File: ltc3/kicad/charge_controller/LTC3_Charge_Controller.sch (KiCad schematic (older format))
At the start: 120 parts, among them P1 MicroFit header, P3 XH header, P4 MicroFit header, P5 XH header, P6 XH header, Q1 ZVN4525E6, Q2 BSC028N06NS, Q3 BSC028N06NS, Q4 BSC028N06NS, Q5 BSC028N06NS, Q6 ZVP3310F, Q7 MMBT5550L, U1 PI2127, U2 PI2127, U3 LT8490, U4 LTC2990

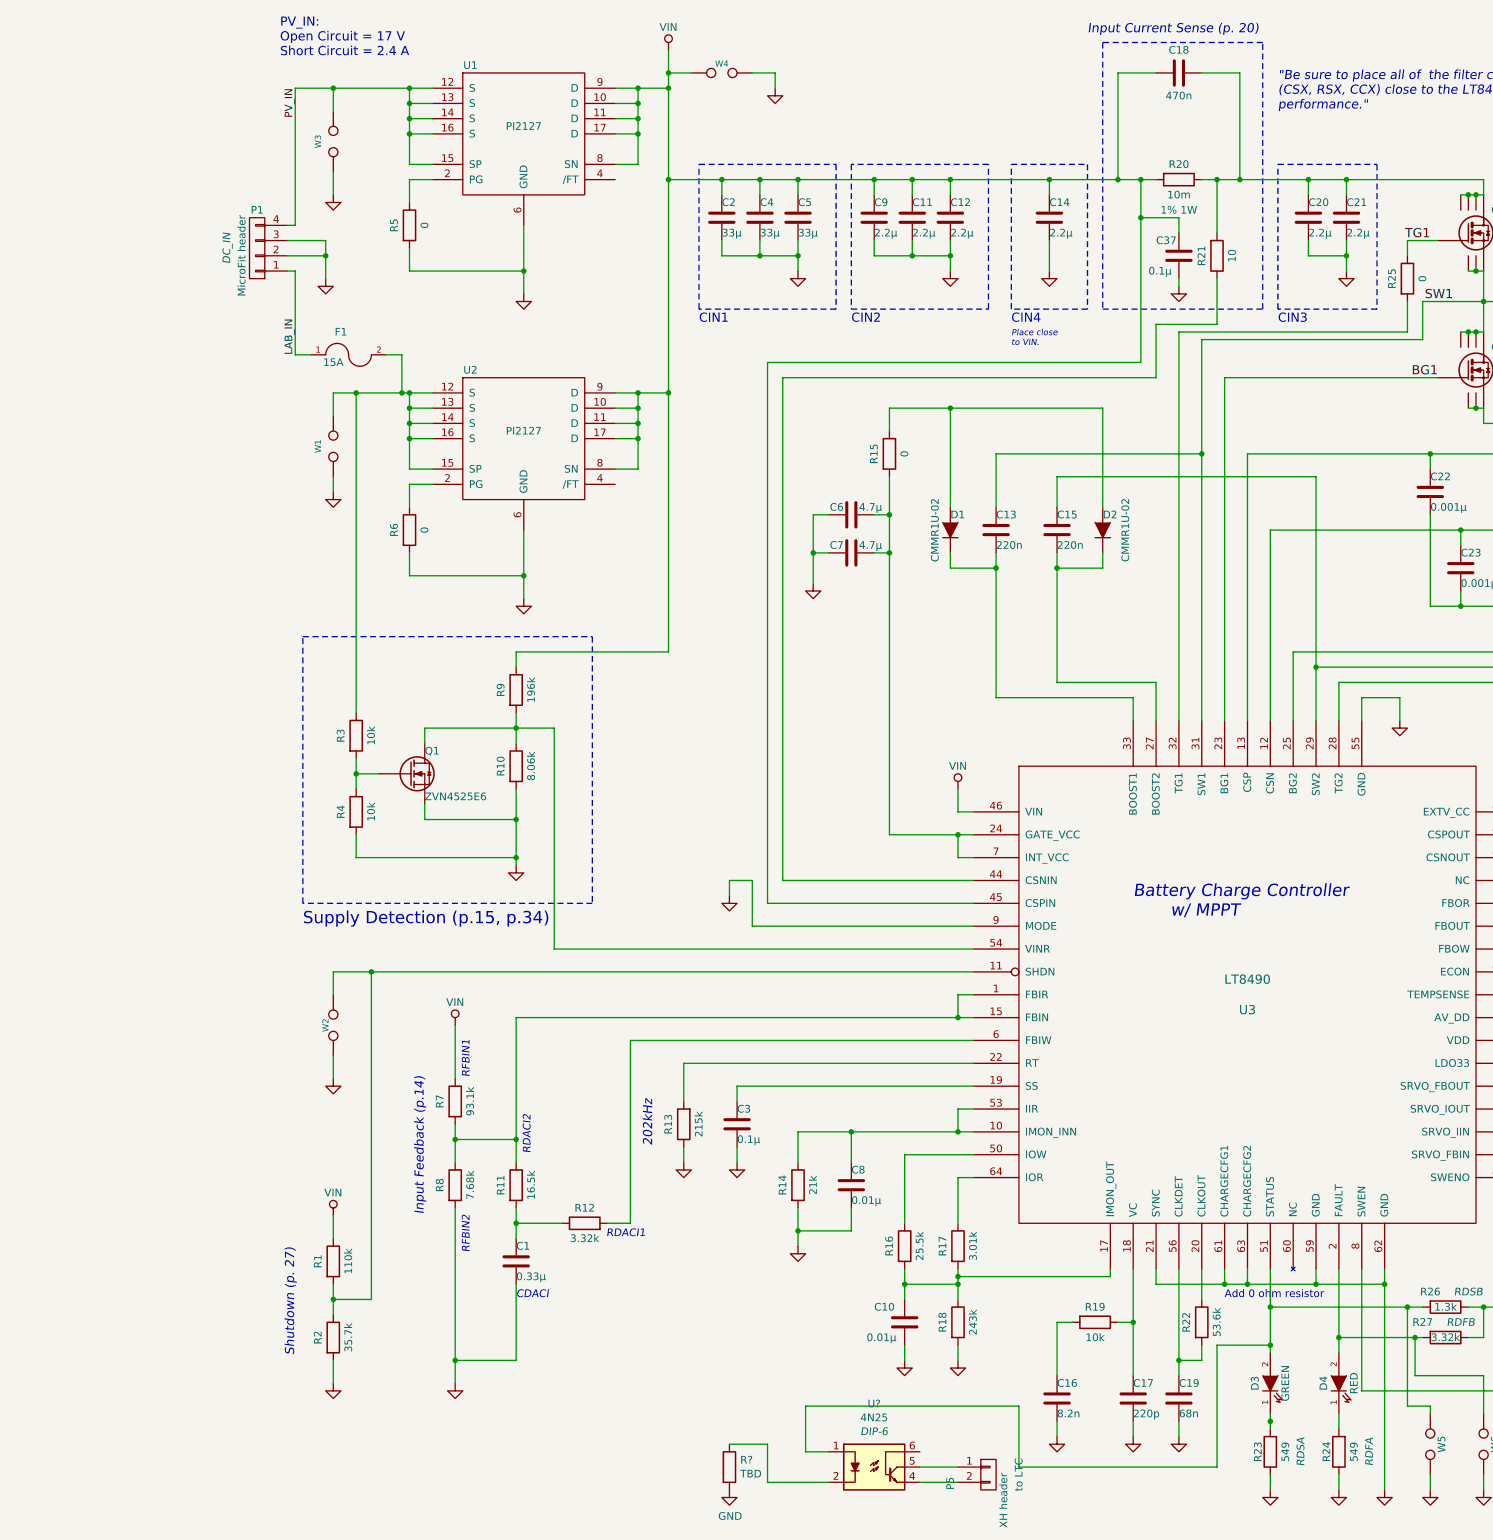
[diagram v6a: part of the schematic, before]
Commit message: LTC3: Layout Review Notes
-Connected pin 4 of connector
-Inserted two zero ohm resistors for SYNC/CHARGECFG2 pin
-Doubled up on input for Charge Controller board
-Added optoisolator to LT8490 board
-Made LTC2990 changes
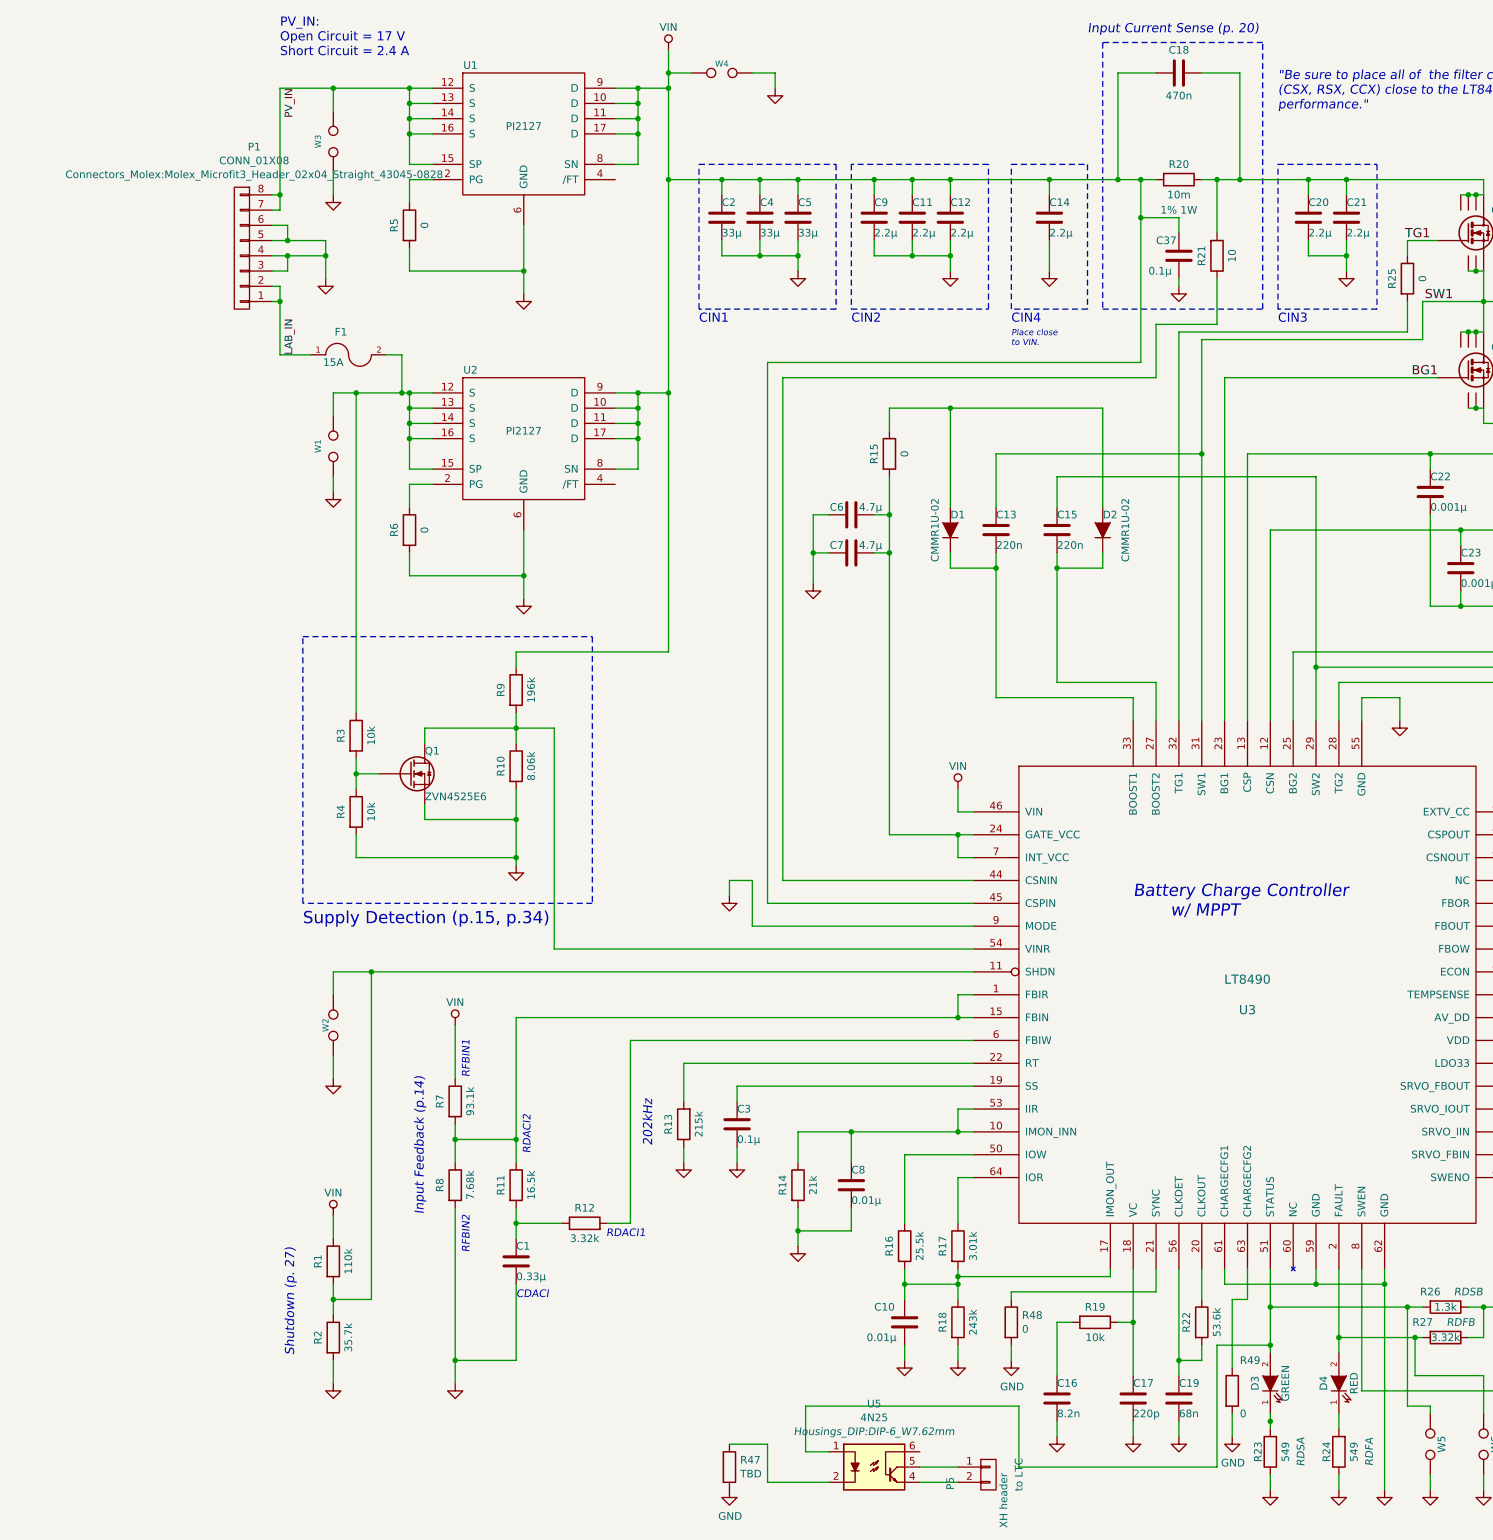
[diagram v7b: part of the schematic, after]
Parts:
- removed P1: MicroFit header, Connectors_Molex:Molex_Microfit3_Header_02x02_Straight_43045-0428, symbol CONN_01X04
- added P1: CONN_01X08, Connectors_Molex:Molex_Microfit3_Header_02x04_Straight_43045-0828, symbol CONN_01X08
- added R48, R49: 0, Resistors_SMD:R_0805, symbol R
- R47: renamed from R?; footprint (none) -> Resistors_SMD:R_0805
- U5: renamed from U?; footprint DIP-6 -> Housings_DIP:DIP-6_W7.62mm
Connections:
- net GND: now also P1.3 (P3), P1.4 (P4), P1.5 (P5), P1.6 (P6), R48.2, R49.2; no longer U3.21 (SYNC), U3.63 (CHARGECFG2)
- net LAB_IN: now also P1.1 (P1), P1.2 (P2)
- net PV_IN: now also P1.7 (P7), P1.8 (P8)
- new net: R48.1, U3.21 (SYNC)
- new net: R49.1, U3.63 (CHARGECFG2)
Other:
- note removed: "Add 0 ohm resistor"

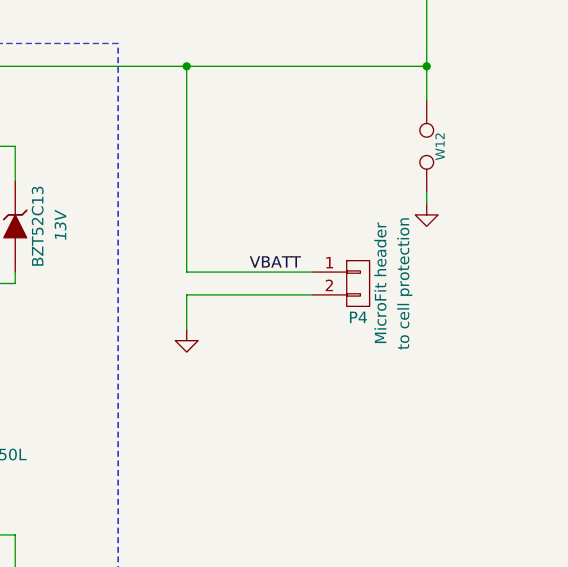
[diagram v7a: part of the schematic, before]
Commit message: LTC3: Charge Controller/Cell Protection Connectors
Upadated connector footrpints on all in/outs to support higher current.

Will export Gerber files later this afternoon.
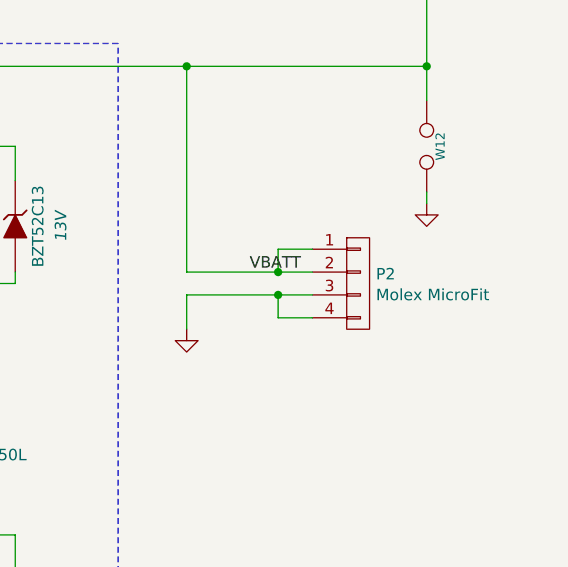
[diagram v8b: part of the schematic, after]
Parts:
- removed P4: MicroFit header, Connectors_Molex:Molex_Microfit3_Header_02x01_Straight_43045-0228, symbol CONN_01X02
- added P2: Molex MicroFit, Connectors_Molex:Molex_Microfit3_Header_02x02_Straight_43045-0428, symbol CONN_01X04
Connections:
- net GND: now also P2.3 (P3), P2.4 (P4)
- net VBATT: now also P2.1 (P1), P2.2 (P2)
